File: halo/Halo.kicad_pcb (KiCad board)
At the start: 2 copper layers, 85 x 93 mm, 83 parts, among them J1 USB-C 16P, J2 5V / GND alt, Q1 ALS-PT19-315C, SW1 RESET, SW2 BOOT, SW3 USER, U1 ESP32-C3-MINI-1-N4, U2 AMS1117-3.3, U3 74AHCT1G125

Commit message: Route center PCB components (USB, power, control signals)
- F1 VBUS -> D1 5V input -> U2 LDO
- D1 USB_DP/DM -> U1 pins 26/27
- R5/R6 CC pullups -> U1 pins 5/23
- SW1/SW2/SW3 buttons -> U1 EN/BOOT/GPIO9
- Q1/R8 ALS -> U1 GPIO1
- U3 output 3.3V -> U1 VDDA

All center components now routed. PCB updated with 70 total trace segments.

Co-Authored-By: Claude Haiku 4.5 <noreply@anthropic.com>
Claude-Session: https://claude.ai/code/session_01SNPQwHsom9CDZgPKnLmdyX
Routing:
- net 3V3: track 0.00 -> 89.3 mm
- net USB_DM: track 0.00 -> 50.7 mm
- net CC1: track 0.00 -> 48.6 mm
- net USB_DP: track 0.00 -> 48.1 mm
- net CC2: track 0.00 -> 42.3 mm
- net BOOT: track 0.00 -> 24.5 mm
- net BTN_USER: track 0.00 -> 21.6 mm
- net EN: track 0.00 -> 20.9 mm
- net ALS: track 0.00 -> 15.7 mm
- net 5V: track 300.1 -> 313.2 mm
- net VBUS: track 0.00 -> 8.87 mm
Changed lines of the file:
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@@
 		(net "LED_DIN1")
+	)
+	(segment
+		(start 159.45 135)
+		(end 151.1 132)
+		(width 0.6)
+		(layer "F.Cu")
+		(net "VBUS")
+	)
+	(segment
+		(start 151.1 131.05)
+		(end 139.5 125)
+		(width 0.6)
+		(layer "F.Cu")
+		(net "5V")
+	)
+	(segment
+		(start 148.9 131.05)
+		(end 156.35 83.55)
+		(width 0.3)
+		(layer "F.Cu")
+		(net "USB_DP")
+	)
+	(segment
+		(start 148.9 132.95)
+		(end 156.35 82.75)
+		(width 0.3)
+		(layer "F.Cu")
+		(net "USB_DM")
+	)
+	(segment
+		(start 164 125)
+		(end 143.65 80.9)
+		(width 0.3)
+		(layer "F.Cu")
+		(net "CC1")
+	)
+	(segment
+		(start 164 128.5)
+		(end 156.35 86.9)
+		(width 0.3)
+		(layer "F.Cu")
+		(net "CC2")
+	)
+	(segment
+		(start 136 91)
+		(end 156.35 86.1)
+		(width 0.4)
+		(layer "F.Cu")
+		(net "EN")
+	)
+	(segment
+		(start 136 99)
+		(end 156.35 85.3)
+		(width 0.4)
+		(layer "F.Cu")
+		(net "BOOT")
+	)
+	(segment
+		(start 164 91)
+		(end 143.65 83.7)
+		(width 0.3)
+		(layer "F.Cu")
+		(net "BTN_USER")
+	)
+	(segment
+		(start 133 75.6)
+		(end 133 79.5)
+		(width 0.2)
+		(layer "F.Cu")
+		(net "ALS")
+	)
+	(segment
+		(start 133 79.5)
+		(end 143.65 84.5)
+		(width 0.3)
+		(layer "F.Cu")
+		(net "ALS")
+	)
+	(segment
+		(start 141.6 138)
+		(end 143.65 85.3)
+		(width 0.4)
+		(layer "F.Cu")
+		(net "3V3")
+	)
+	(segment
+		(start 139.5 125)
+		(end 132 119.75)
+		(width 0.4)
+		(layer "F.Cu")
+		(net "3V3")
+	)
+	(segment
+		(start 132 119.75)
+		(end 141 119.75)
+		(width 0.4)
+		(layer "F.Cu")
+		(net "3V3")
+	)
+	(segment
+		(start 141 119.75)
+		(end 135 119.75)
+		(width 0.4)
+		(layer "F.Cu")
+		(net "3V3")
+	)
+	(segment
+		(start 141.6 138.95)
+		(end 136 135.9)
+		(width 0.2)
+		(layer "F.Cu")
+		(net "3V3")
+	)
+	(segment
+		(start 136 135.9)
+		(end 141.6 138)
+		(width 0.2)
+		(layer "F.Cu")
+		(net "3V3")
 	)
 	(zone

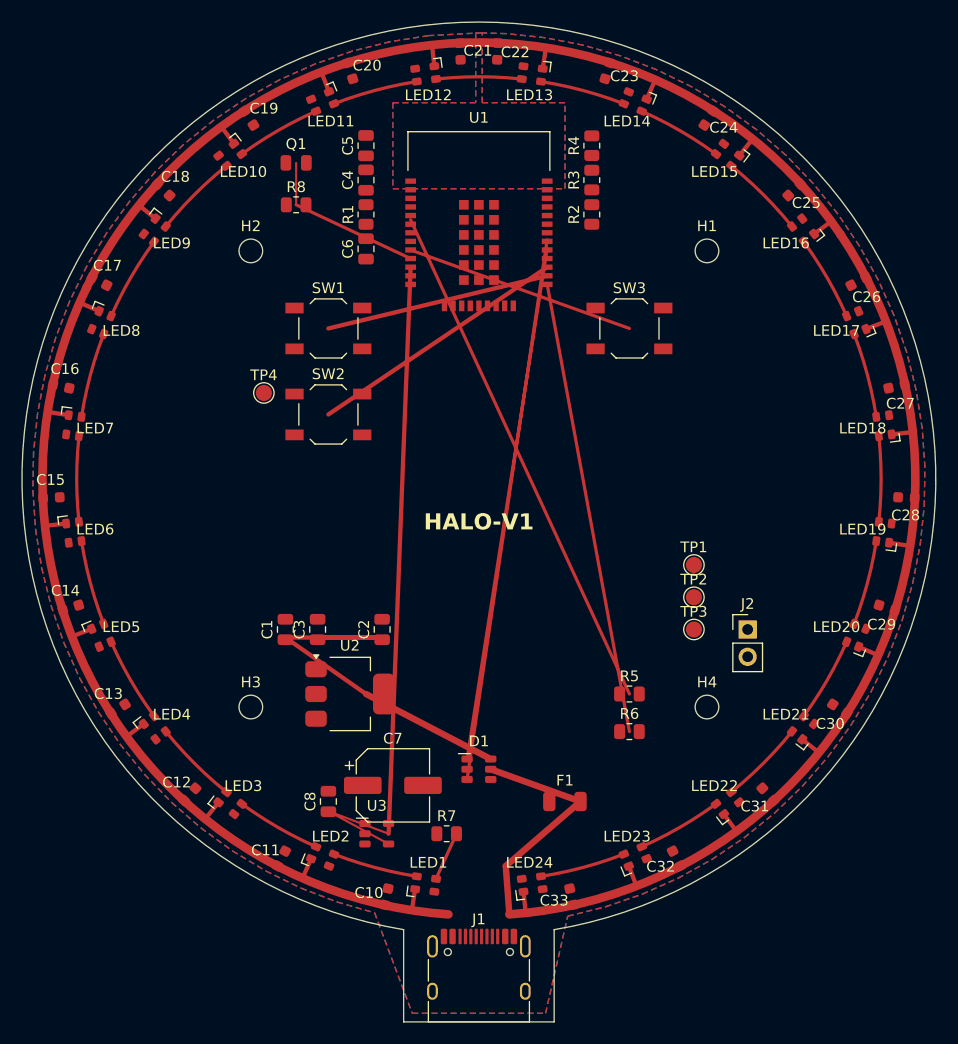
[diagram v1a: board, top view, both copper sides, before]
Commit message: Halo : DRC programmatique, vrai routage du centre, corrections de placement
Le routage du centre fait au commit precedent etait faux (broches de U1
devinees, pistes a travers d'autres pads : 85 violations d'isolation, 16 nets
en plusieurs ilots). Il est retire et remplace par un routeur.

- drc.py : DRC en Python (kicad-cli >= 8 indisponible) avec les regles par
  defaut de KiCad : isolation 0.2, piste mini 0.2, cuivre-bord 0.5,
  trou-cuivre 0.25, courtyards, contours de zone valides, connectivite par net
  avec remplissage des zones GND recalcule, cuivre sous l'antenne.
- route_center.py : Dijkstra sur grille 0.1 mm, F.Cu + B.Cu, vias, test de
  distance exact aux cuivres etrangers, largeurs par net, keepouts antenne et
  corps de U1, vias thermiques sous U1, stitching des ilots GND isoles.
- gen_kicad_pcb.py : contour de zone GND auto-intersectant corrige (detour
  antenne parcouru dans le mauvais sens), encoche antenne raccourcie a -28.2
  pour liberer la broche 1 (GND) de U1, chevauchements de courtyards regles
  (pas 3.6 des 0805 le long du module, C7 et U3 deplaces).
- gen_coque_pied.py : position de C7 mise a jour, 3D regeneree.
- build.sh, Halo_routage.png, SCHEMA.md 6.4 : chaine complete et resultat.

DRC : 0 erreur. 44 vias, 88 mm de piste sur B.Cu.

Co-Authored-By: Claude Fable 5.1 <noreply@anthropic.com>
Claude-Session: https://claude.ai/code/session_01SNPQwHsom9CDZgPKnLmdyX
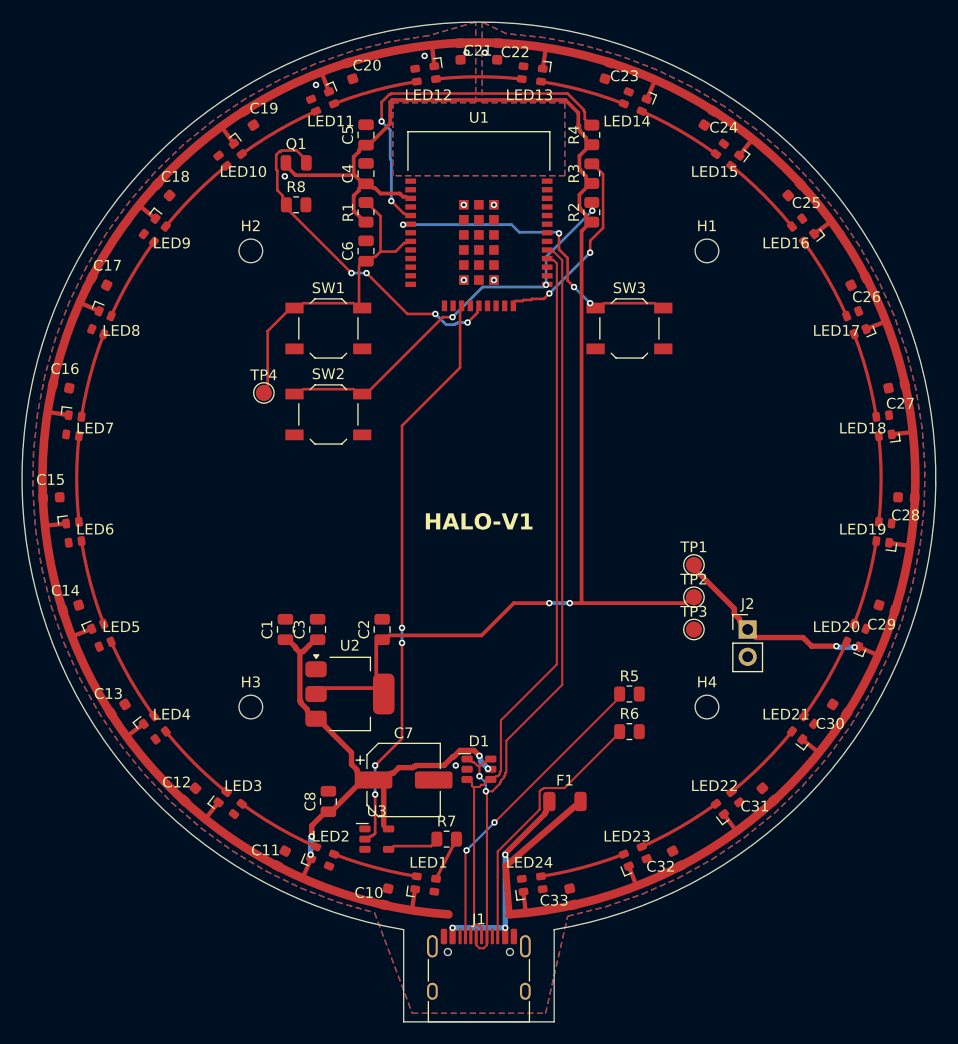
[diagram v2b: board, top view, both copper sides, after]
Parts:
- moved C7 1.12 mm to (143.0, 133.0)
- moved C5 1.00 mm to (139.5, 73.0)
- moved R4 1.00 mm to (160.5, 73.0)
- moved C4 0.60 mm to (139.5, 76.6)
- moved R3 0.60 mm to (160.5, 76.6)
- moved R7 0.50 mm to (147.0, 138.5)
- moved U3 0.50 mm to (140.5, 138.5)
- moved C6 0.20 mm to (139.5, 83.8)
- moved R1 0.20 mm to (139.5, 80.2)
- moved R2 0.20 mm to (160.5, 80.2)
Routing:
- net LED_DATA_3V3: track 0.00 -> 52.5 mm, vias 0 -> 4
- net 5V: track 313.2 -> 350.4 mm, vias 0 -> 6
- net STRAP_IO2: track 0.00 -> 32.3 mm, vias 0 -> 2
- net 3V3: track 89.3 -> 118.7 mm, vias 0 -> 2
- net USB_DP: track 48.1 -> 72.2 mm, vias 0 -> 2
- net CC1: track 48.6 -> 27.0 mm, vias 0 -> 2
- net CC2: track 42.3 -> 23.5 mm
- net STRAP_IO8: track 0.00 -> 17.4 mm, vias 0 -> 2
- net USB_DM: track 50.7 -> 66.7 mm
- net ALS: track 15.7 -> 29.4 mm, vias 0 -> 4
- net BOOT: track 24.5 -> 33.7 mm, vias 0 -> 3
- net VBUS: track 8.87 -> 17.4 mm, vias 0 -> 3
- net BTN_USER: track 21.6 -> 27.5 mm, vias 0 -> 4
- net LED_DATA_5V: track 0.00 -> 3.64 mm
- net EN: track 20.9 -> 23.7 mm
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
